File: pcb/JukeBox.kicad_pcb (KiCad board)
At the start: 2 copper layers, 102 x 100 mm, 102 parts, among them J1 USB_C_Receptacle_USB2.0_16P, Q1 Q_NPN_BEC, SW1 SW_SPST, SW10 SW_SPST, SW11 SW_SPST, SW12 SW_SPST, SW13 SW_SPST, SW2 SW_SPST, SW3 SW_SPST, SW4 SW_SPST, SW5 SW_SPST, SW6 SW_SPST, SW7 SW_SPST, SW8 SW_SPST, SW9 SW_SPST, U1 NCP1117-3.3_SOT223, U2 W25Q128JVS, U3 RP2350_60QFN, U5 CAT24C512, Y1 ABM8-272-T3

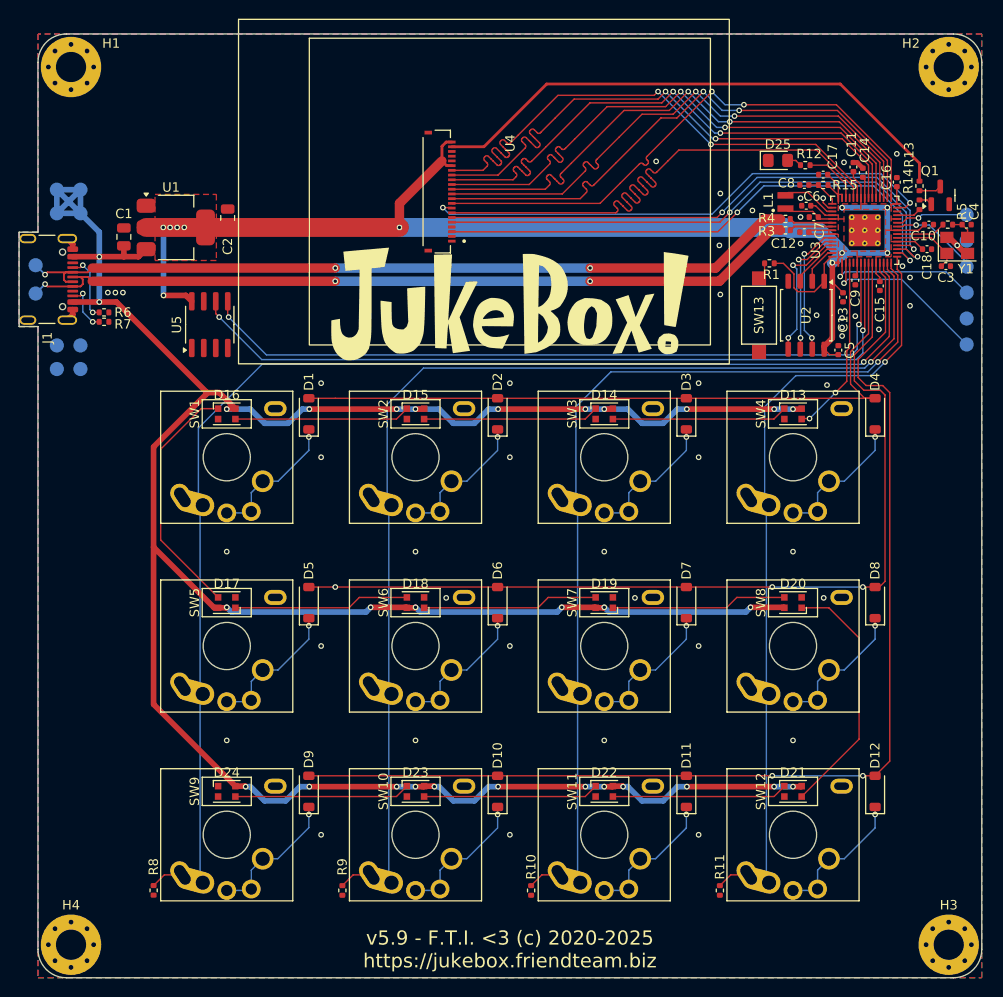
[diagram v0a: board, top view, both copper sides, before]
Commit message: shorten pcb to reduce cost
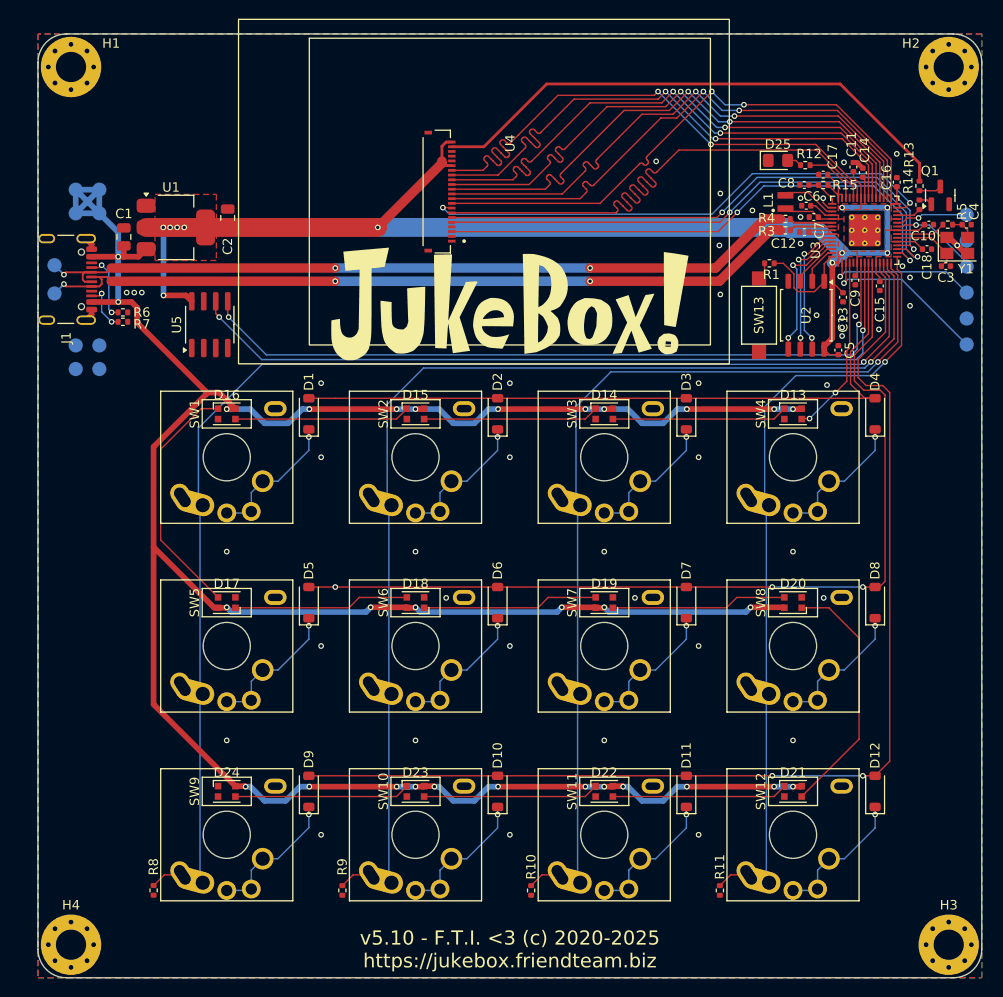
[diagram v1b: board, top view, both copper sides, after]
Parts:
- moved J1 2.00 mm to (64.6, 93.0)
- moved R6 2.00 mm to (71.6, 96.5)
- moved R7 2.00 mm to (71.6, 97.5)
- moved TP10 2.00 mm to (64.3, 94.5)
- moved TP11 2.00 mm to (64.3, 91.5)
- moved TP12 2.00 mm to (69.1, 83.5)
- moved TP13 2.00 mm to (69.1, 86.0)
- moved TP14 2.00 mm to (66.6, 86.0)
- moved TP15 2.00 mm to (66.6, 83.5)
- moved TP16 2.00 mm to (69.1, 100.0)
- moved TP17 2.00 mm to (66.6, 100.0)
- moved TP18 2.00 mm to (69.1, 102.5)
- moved TP19 2.00 mm to (66.6, 102.5)
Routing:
- net VBUS: track 308.3 -> 305.2 mm
- net /USB_D-: track 84.4 -> 82.4 mm
- net /USB_D+: track 83.9 -> 81.9 mm
- net +3V3: track 158.6 -> 159.6 mm
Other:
- board size 102 x 100 mm -> 100 x 100 mm
- board text added: "v5.10 - F.T.I. <3 (c) 2020-2025 https://jukebox.friendteam.biz"
- board text removed: "v5.9 - F.T.I. <3 (c) 2020-2025 https://jukebox.friendteam.biz"
